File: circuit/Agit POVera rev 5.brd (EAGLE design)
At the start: 39.5 x 81.9 mm, 37 parts, among them IC1 MEGA8-P, J1 AVR_SPI_PRG_6NS, Y2 8Mhz

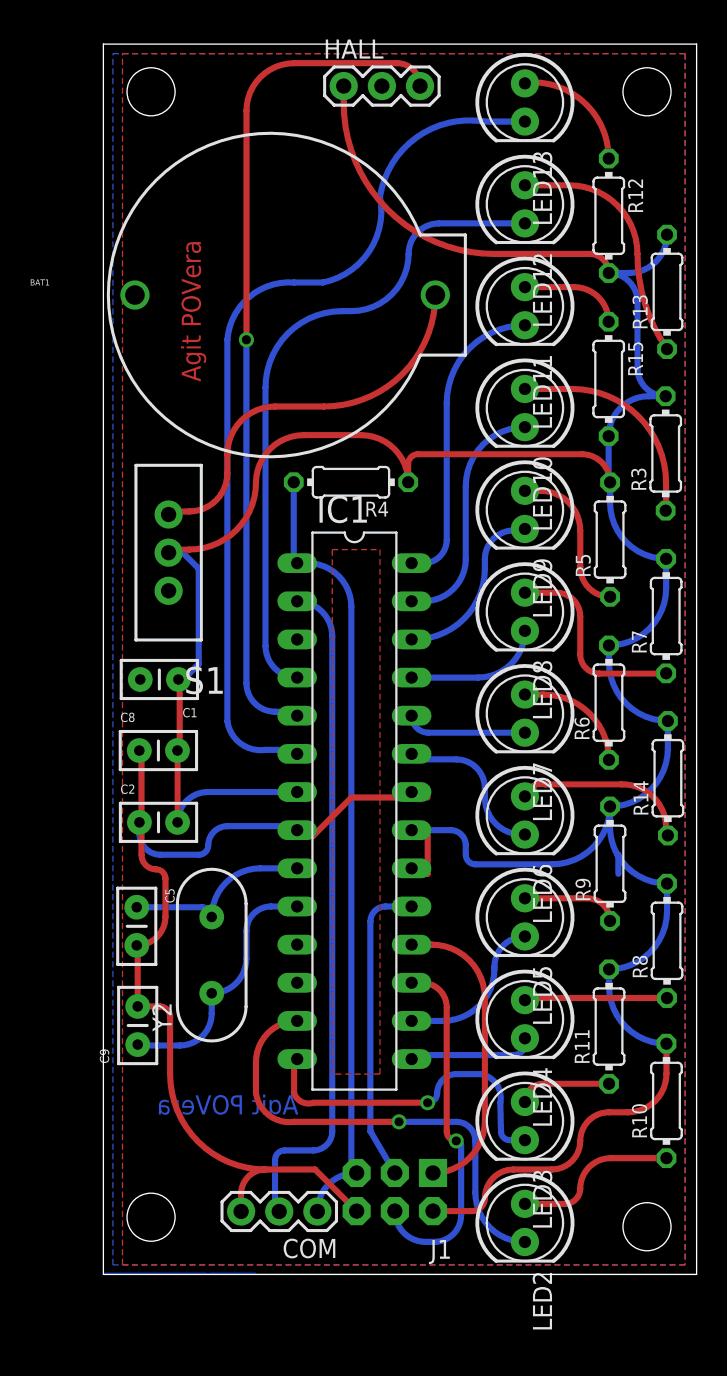
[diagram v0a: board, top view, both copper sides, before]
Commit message: Changes for rev 5
Everything new is under ‘circuit’  :
The build guide is updated;
Removed the extra parts in the BOM;
Added the new version of the .brd, .sch and the gerbers for people
wanting to print more from board houses.
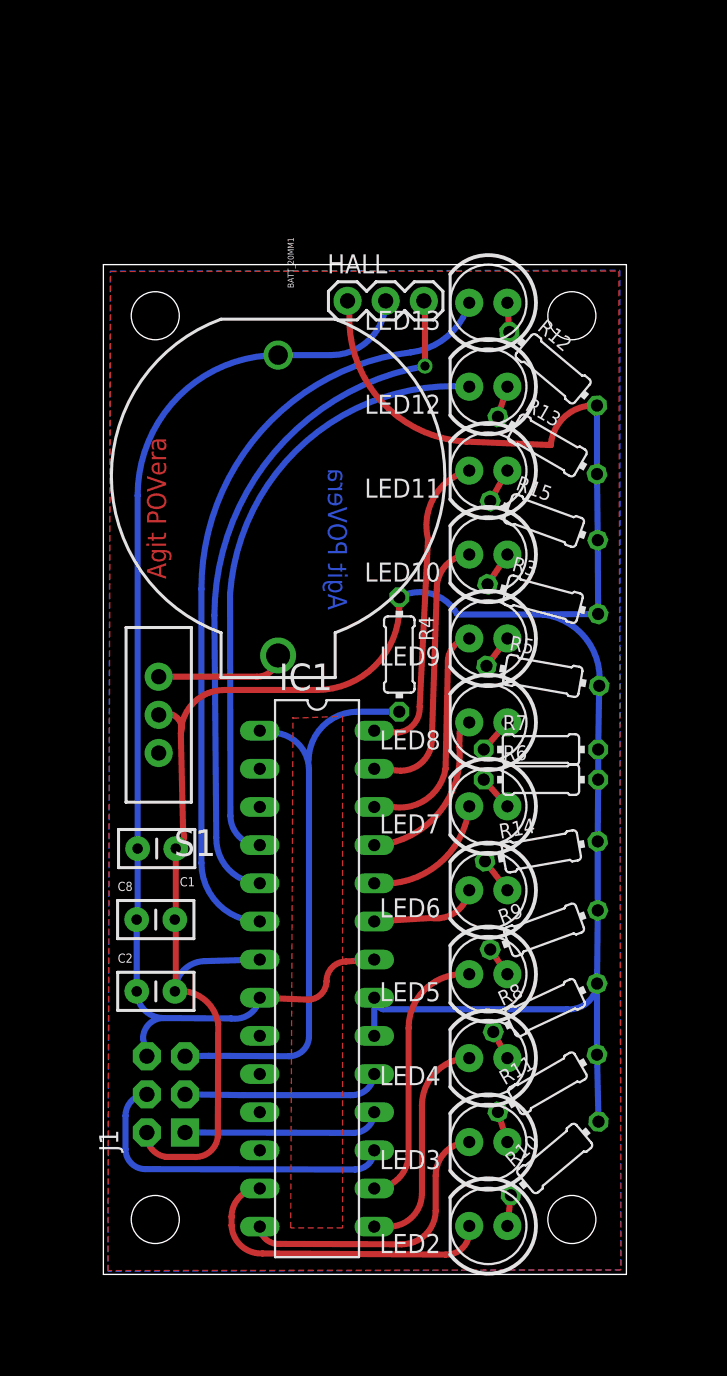
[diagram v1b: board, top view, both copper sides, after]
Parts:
- removed BAT1: (no value), SparkFun-Electromechanical:BATTCOM_20MM_PTH
- removed C5, C9: 27pF, SparkFun-Passives:CAP-PTH-SMALLEZ
- removed COM: (no value), SparkFun-Connectors:1X03
- removed Y2: 8Mhz, SparkFun-FreqCtrl:HC49US
- added BATT_20MM1: (no value), User-Submitted:BATTERIE
- R13, R3, R6: value 60 -> 47
- R14: value 60 -> 45
- moved J1 16.6 mm to (4.17, 12.0), turned to 90 degrees
- moved HALL 14.3 mm to (16.3, 64.8)
- moved LED13 13.6 mm to (25.6, 64.7), turned to 180 degrees
- moved R13 13.0 mm to (29.6, 55.2), turned to 330 degrees
- moved R3 12.7 mm to (29.3, 45.0), turned to 345 degrees
- moved LED12 12.4 mm to (25.6, 59.1), turned to 180 degrees
- moved R7 12.2 mm to (29.1, 35.0), turned to 0 degrees
- moved R4 11.9 mm to (19.7, 41.3), turned to 270 degrees
- moved IC1 11.4 mm to (14.2, 19.7)
- moved C1 11.3 mm to (4.82, 28.4)
- moved C8 11.3 mm to (2.22, 23.6)
- moved C2 11.3 mm to (2.22, 18.8)
- moved LED11 11.2 mm to (25.6, 53.5), turned to 180 degrees
- moved R12 10.8 mm to (29.9, 60.3), turned to 320 degrees
- moved S1 10.8 mm to (3.68, 37.3)
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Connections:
- net N$1 renamed LED7
- net N$10 renamed LED4
- net N$11 renamed LED5
- net N$12 renamed LED13
- net N$13 renamed R9
- net N$2 renamed LED8
- net N$21 renamed R7
- net N$3 renamed LED9
- net N$4 renamed LED12
- net N$5 renamed LED10
- net N$6 renamed LED11
- net N$7 renamed LED6
- net N$8 renamed LED2
- net N$9 renamed LED3
- removed net N$34: C5.1, IC1.9, Y2.2
- removed net N$35: C9.1, IC1.10, Y2.1
- removed net RX: COM.2, IC1.2
- net GND: now also BATT_20MM1.2; no longer BAT1.2, C5.2, C9.2, COM.3
- net RESET: no longer COM.1
- net V_BATT: now also BATT_20MM1.1; no longer BAT1.1
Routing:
- net RX: track 44.4 -> 0.00 mm
- net 3.3V: track 204.7 -> 164.7 mm
- net N$35: track 16.3 -> 0.00 mm
- net V_BATT: track 24.5 -> 8.54 mm
- net N$15: track 16.0 -> 2.10 mm
- net RESET: track 51.8 -> 38.2 mm
- net N$34: track 12.3 -> 0.00 mm
- net N$22: track 13.9 -> 2.38 mm
- net HALL_OUT: track 56.3 -> 45.0 mm
- net R7: track 13.1 -> 2.39 mm
- net LED2: track 29.8 -> 20.8 mm, vias 1 -> 0
- net N$25: track 11.4 -> 2.44 mm
- net N$18: track 10.7 -> 2.06 mm
- net GND: track 67.6 -> 76.1 mm
- net R9: track 10.0 -> 2.30 mm
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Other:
- board size 39.5 x 81.9 mm -> 34.8 x 67.2 mm
